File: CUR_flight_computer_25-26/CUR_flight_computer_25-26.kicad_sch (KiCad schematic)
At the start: 0 parts

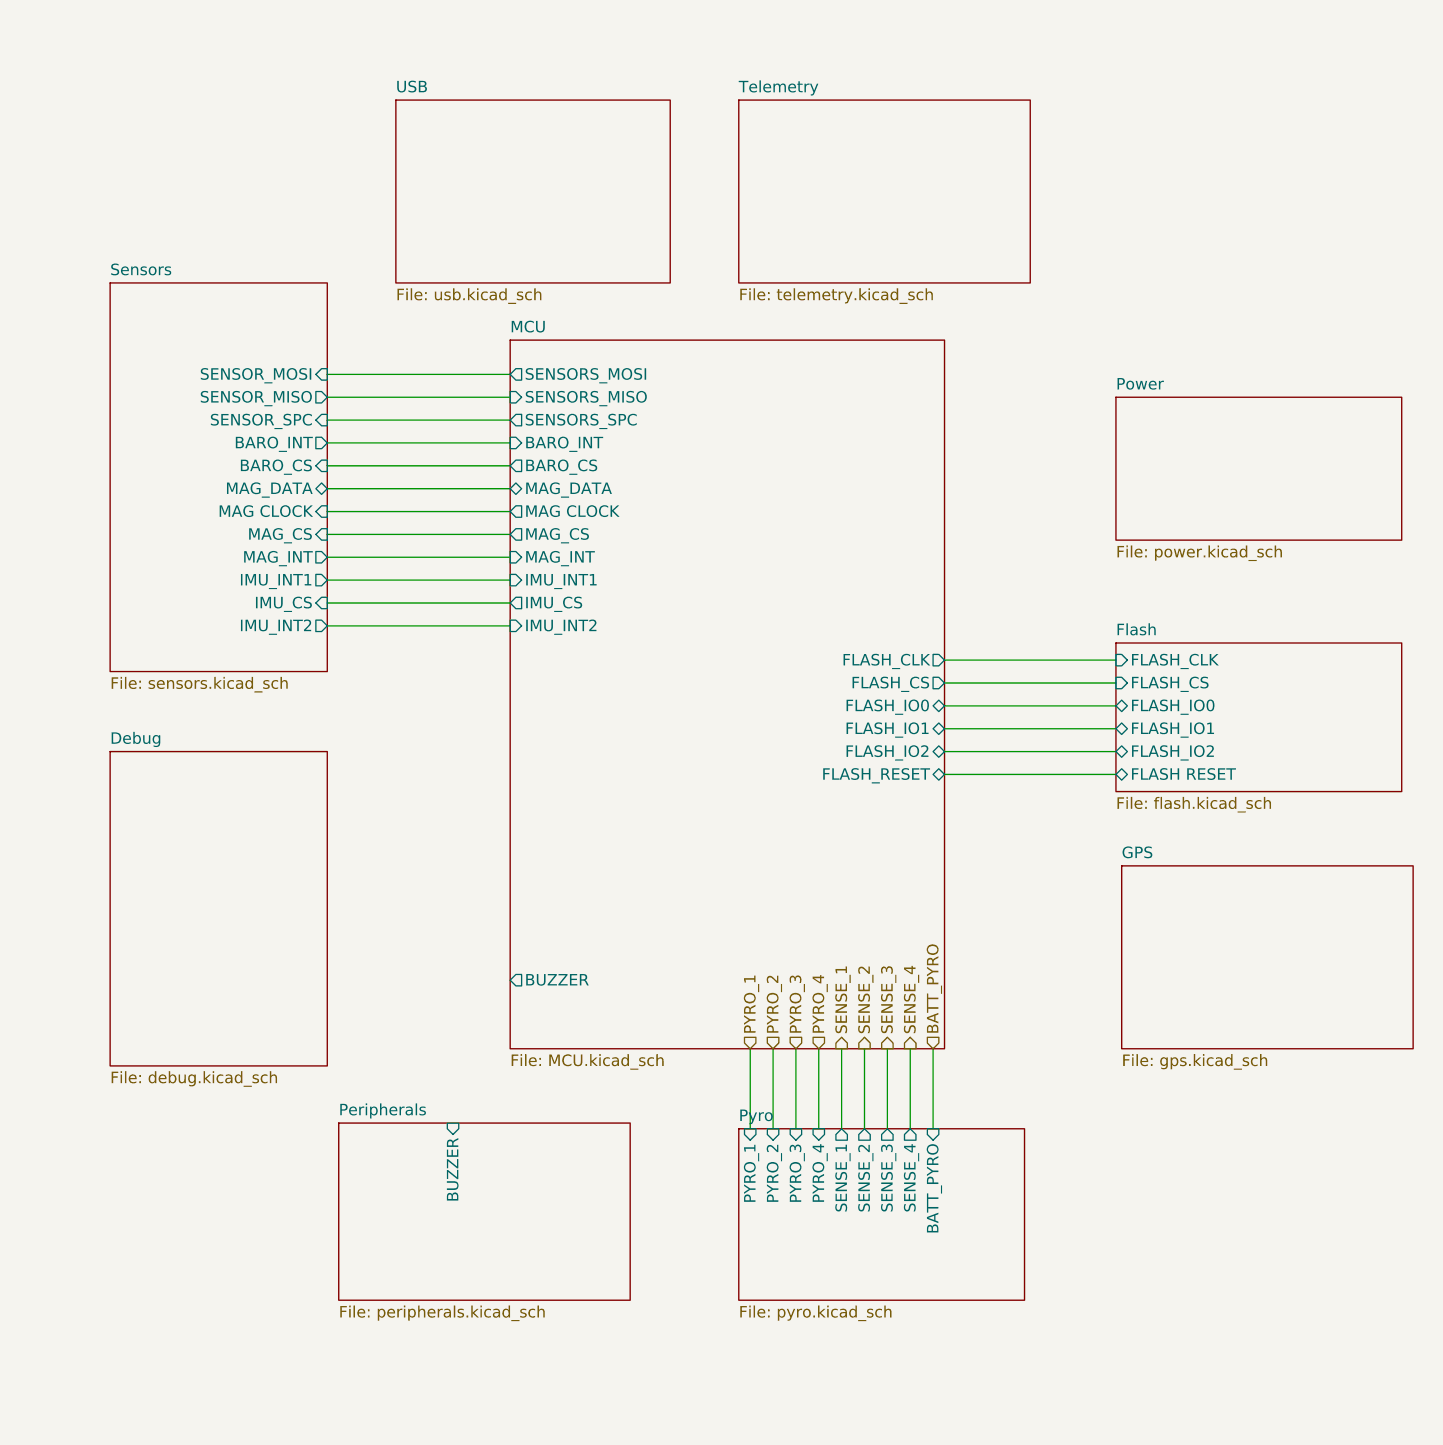
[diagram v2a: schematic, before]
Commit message: updated pins
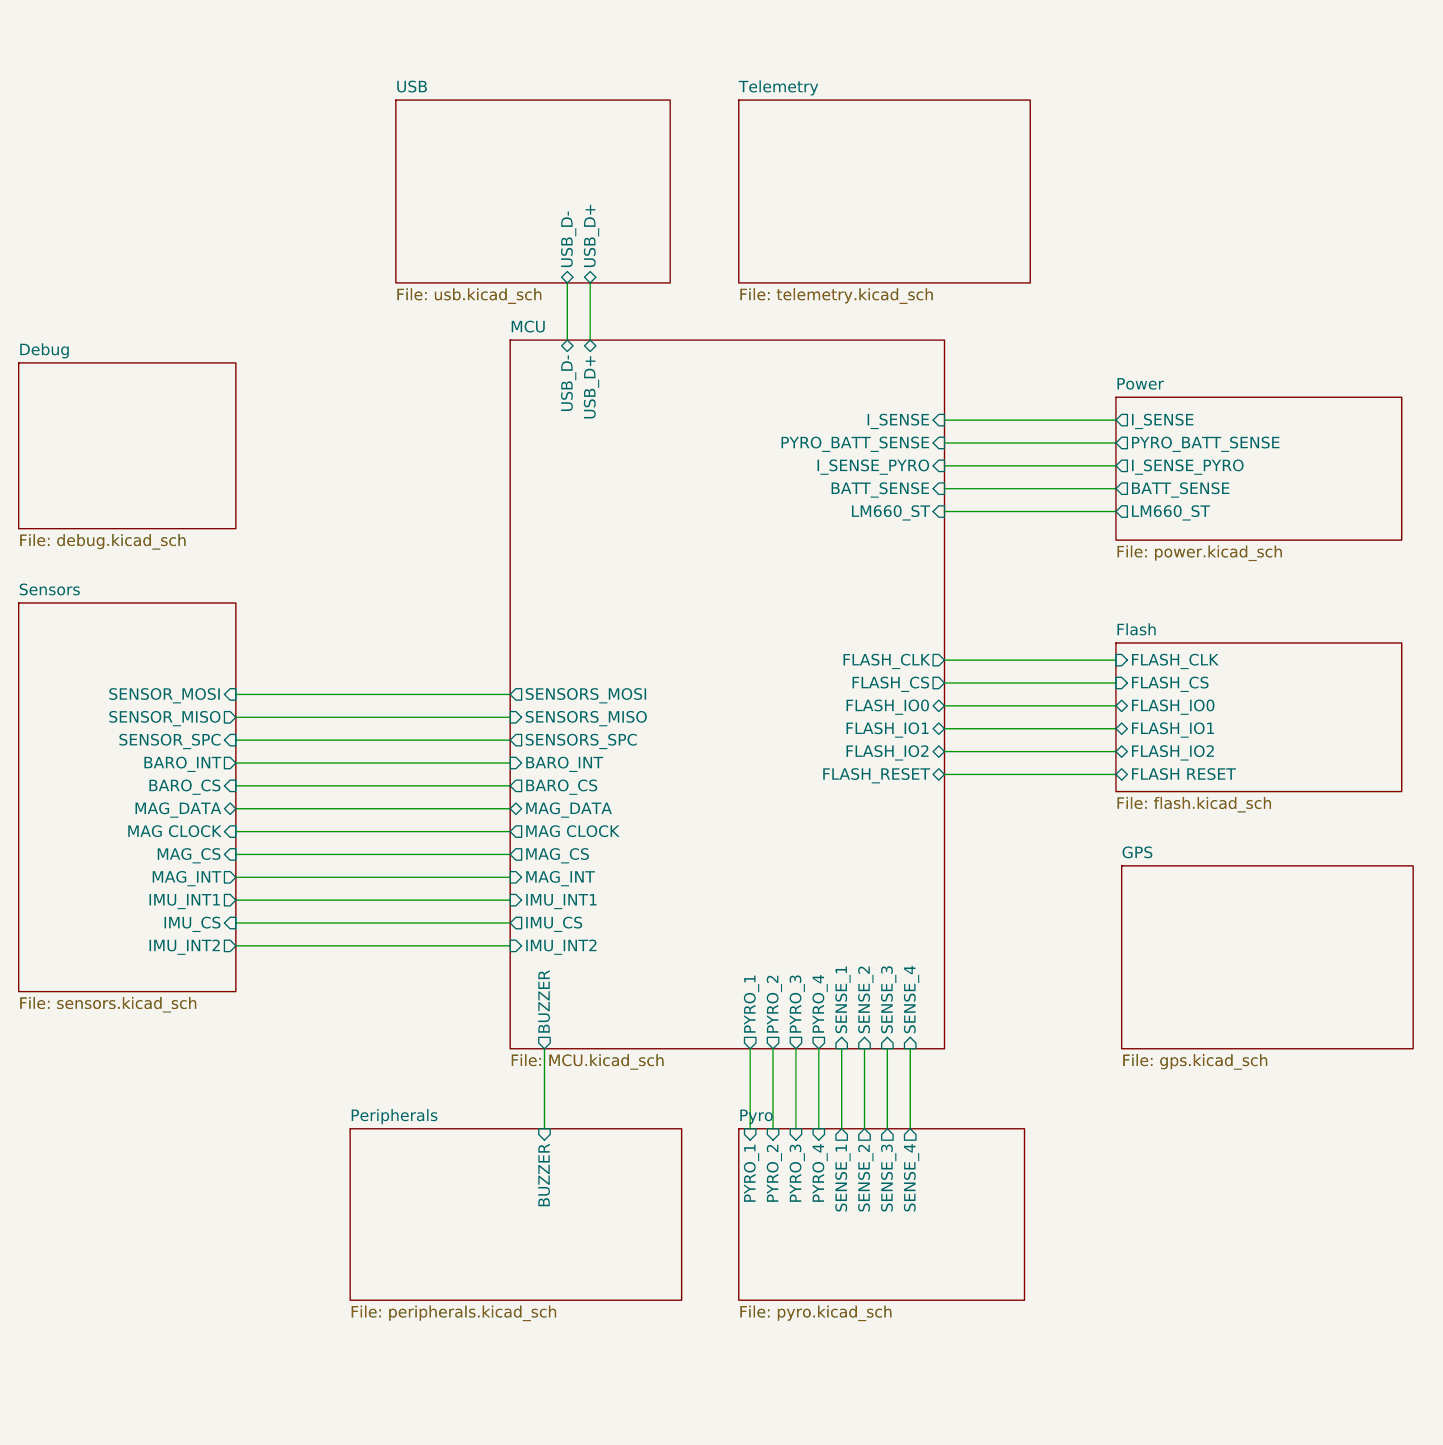
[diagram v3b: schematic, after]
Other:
- sheet MCU ports: added BATT_SENSE, I_SENSE, I_SENSE_PYRO, LM660_ST, PYRO_1, PYRO_2, PYRO_3, PYRO_4, PYRO_BATT_SENSE, SENSE_1, SENSE_2, SENSE_3, SENSE_4, USB_D+, USB_D-; removed none
- sheet Power ports: added BATT_SENSE, I_SENSE, I_SENSE_PYRO, LM660_ST, PYRO_BATT_SENSE; removed none
- sheet Pyro ports: added none; removed BATT_PYRO
- sheet USB ports: added USB_D+, USB_D-; removed none

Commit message: added rf pins
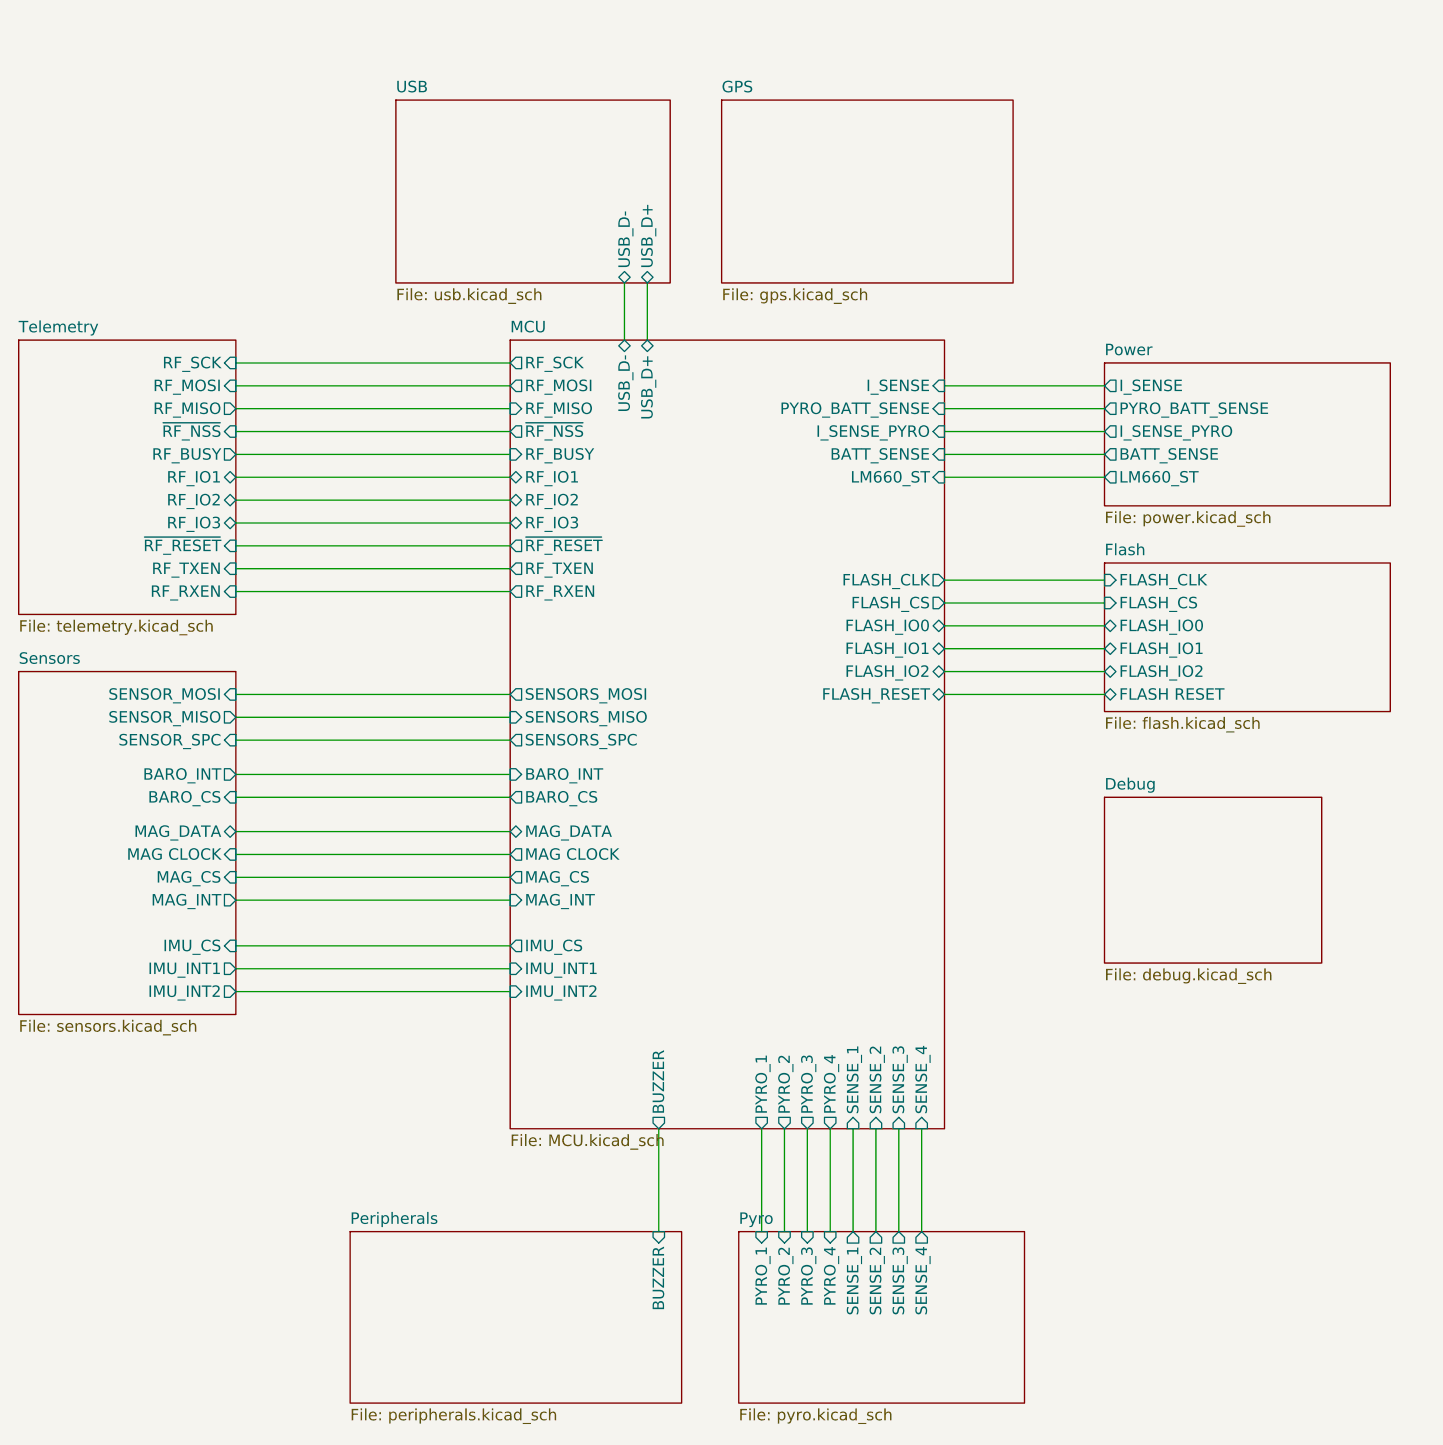
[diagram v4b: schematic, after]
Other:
- sheet MCU ports: added RF_BUSY, RF_IO1, RF_IO2, RF_IO3, RF_MISO, RF_MOSI, RF_RXEN, RF_SCK, RF_TXEN, ~{RF_NSS}, ~{RF_RESET}; removed none
- sheet Telemetry ports: added RF_BUSY, RF_IO1, RF_IO2, RF_IO3, RF_MISO, RF_MOSI, RF_RXEN, RF_SCK, RF_TXEN, ~{RF_NSS}, ~{RF_RESET}; removed none

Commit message: added gps pins
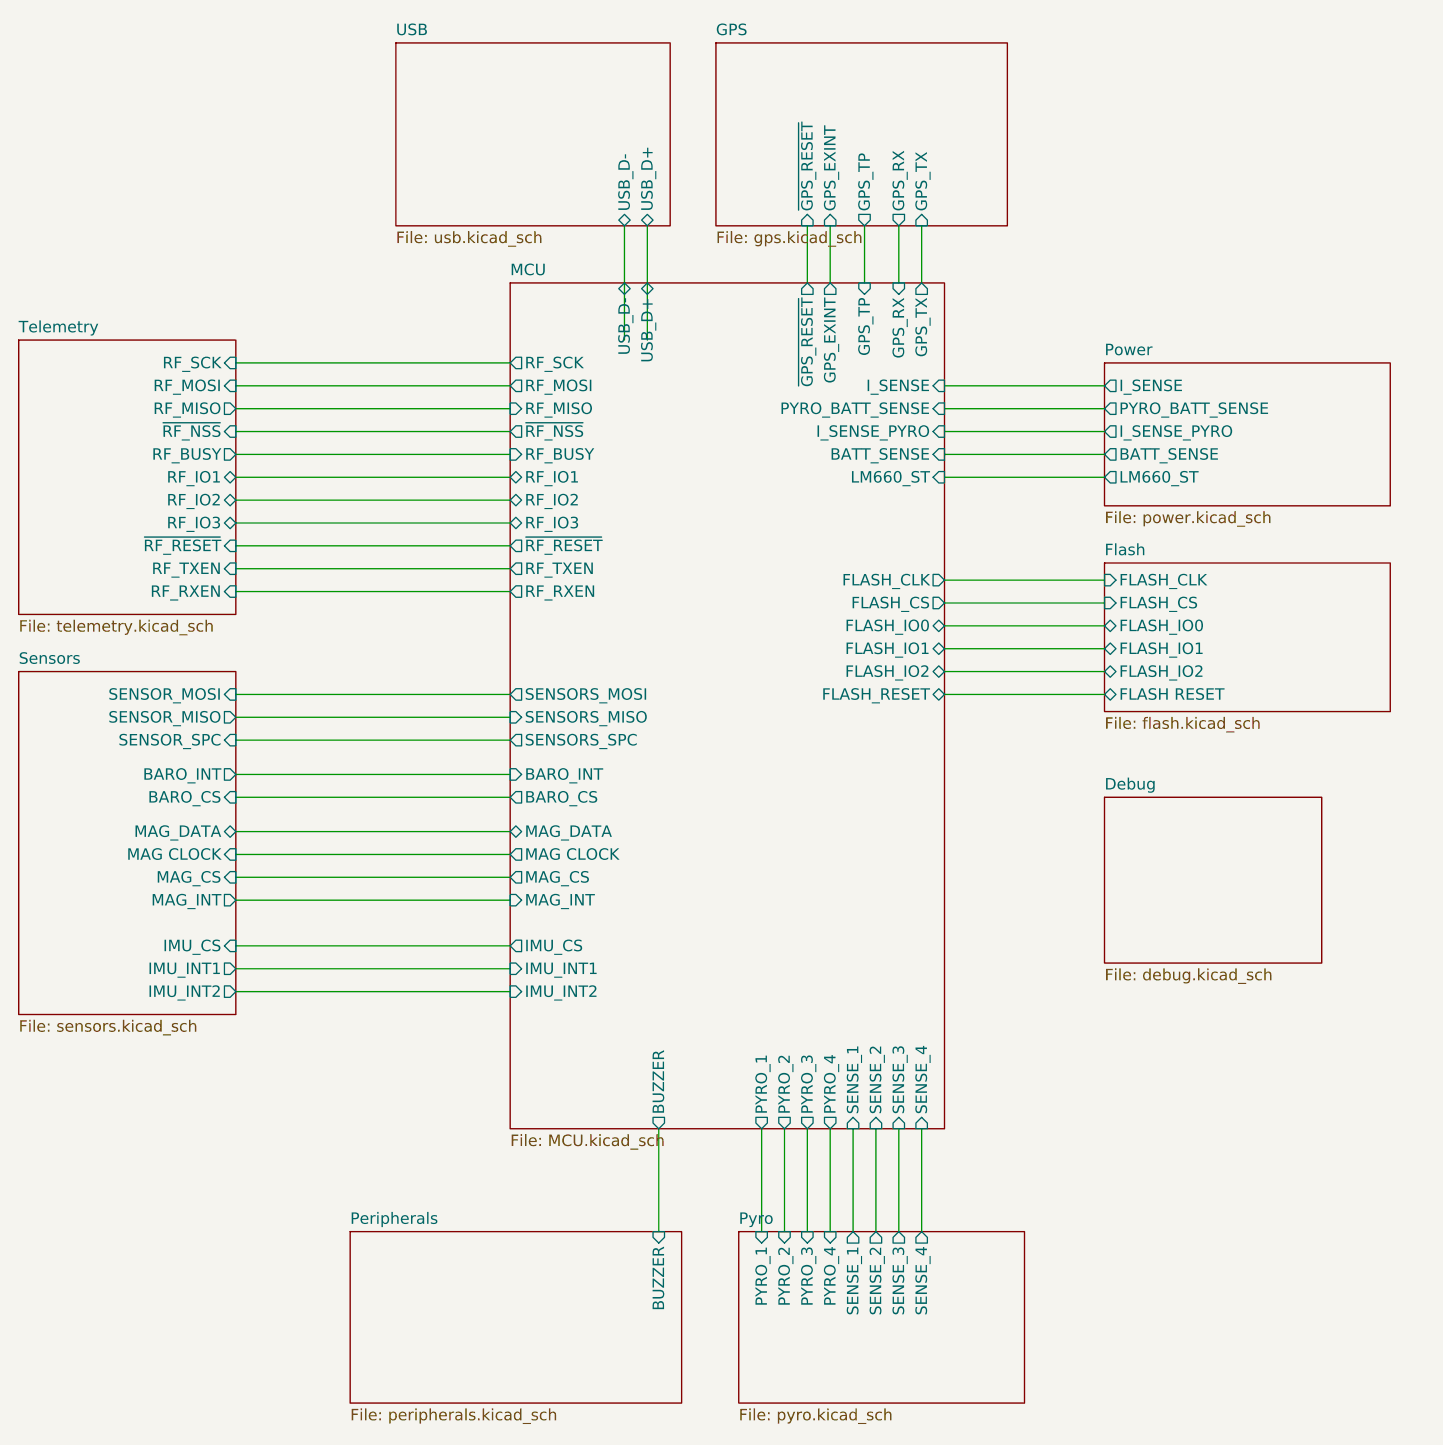
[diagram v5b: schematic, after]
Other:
- sheet GPS ports: added GPS_EXINT, GPS_RX, GPS_TP, GPS_TX, ~{GPS_RESET}; removed none
- sheet MCU ports: added GPS_EXINT, GPS_RX, GPS_TP, GPS_TX, ~{GPS_RESET}; removed none
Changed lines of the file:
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@@
+	(wire
+		(pts
+			(xy 157.48 39.37) (xy 157.48 45.72)
+		)
+		(stroke
+			(width 0)
+			(type default)
+		)
+	)
 	(wire
 		(pts
@@
 	(wire
 		(pts
-			(xy 129.54 45.72) (xy 129.54 52.07)
+			(xy 129.54 39.37) (xy 129.54 52.07)
 		)
 		(stroke
@@
 	(wire
 		(pts
+			(xy 147.32 39.37) (xy 147.32 45.72)
+		)
+		(stroke
+			(width 0)
+			(type default)
+		)
+	)
+	(wire
+		(pts
 			(xy 162.56 86.36) (xy 180.34 86.36)
 		)
@@
 	(wire
 		(pts
+			(xy 153.67 39.37) (xy 153.67 45.72)
+		)
+		(stroke
+			(width 0)
+			(type default)
+		)
+	)
+	(wire
+		(pts
 			(xy 83.82 57.15) (xy 114.3 57.15)
 		)
@@
 	(wire
 		(pts
+			(xy 149.86 39.37) (xy 149.86 45.72)
+		)
+		(stroke
+			(width 0)
+			(type default)
+		)
+	)
+	(wire
+		(pts
 			(xy 83.82 54.61) (xy 114.3 54.61)
 		)
@@
 	(wire
 		(pts
+			(xy 127 39.37) (xy 127 52.07)
+		)
+		(stroke
+			(width 0)
+			(type default)
+		)
+	)
+	(wire
+		(pts
 			(xy 162.56 83.82) (xy 180.34 83.82)
 		)
@@
 	(wire
 		(pts
-			(xy 127 45.72) (xy 127 52.07)
+			(xy 160.02 39.37) (xy 160.02 45.72)
 		)
 		(stroke
@@
 	)
 	(sheet
-		(at 114.3 52.07)
-		(size 48.26 87.63)
+		(at 114.3 45.72)
+		(size 48.26 93.98)
 		(exclude_from_sim no)
 		(in_bom yes)
@@
 		)
 		(property "Sheetname" "MCU"
-			(at 114.3 51.3584 0)
+			(at 114.3 45.0084 0)
 			(effects
 				(font
@@
 		)
 		(pin "USB_D-" bidirectional
-			(at 127 52.07 90)
+			(at 127 45.72 90)
 			(effects
 				(font
@@
 		)
 		(pin "USB_D+" bidirectional
-			(at 129.54 52.07 90)
+			(at 129.54 45.72 90)
 			(effects
 				(font
@@
 				)
 				(justify left)
+			)
+		)
+		(pin "GPS_RX" input
+			(at 157.48 45.72 90)
+			(effects
+				(font
+					(size 1.27 1.27)
+				)
+				(justify right)
+			)
+		)
+		(pin "~{GPS_RESET}" output
+			(at 147.32 45.72 90)
+			(effects
+				(font
+					(size 1.27 1.27)
+				)
+				(justify right)
+			)
+		)
+		(pin "GPS_TX" output
+			(at 160.02 45.72 90)
+			(effects
+				(font
+					(size 1.27 1.27)
+				)
+				(justify right)
+			)
+		)
+		(pin "GPS_TP" input
+			(at 153.67 45.72 90)
+			(effects
+				(font
+					(size 1.27 1.27)
+				)
+				(justify right)
+			)
+		)
+		(pin "GPS_EXINT" output
+			(at 149.86 45.72 90)
+			(effects
+				(font
+					(size 1.27 1.27)
+				)
+				(justify right)
 			)
 		)
@@
 	)
 	(sheet
-		(at 101.6 25.4)
+		(at 101.6 19.05)
 		(size 30.48 20.32)
 		(exclude_from_sim no)
@@
 		)
 		(property "Sheetname" "USB"
-			(at 101.6 24.6884 0)
+			(at 101.6 18.3384 0)
 			(effects
 				(font
@@
 		)
 		(property "Sheetfile" "usb.kicad_sch"
-			(at 101.6 46.3046 0)
+			(at 101.6 39.9546 0)
 			(effects
 				(font
@@
 		)
 		(pin "USB_D+" bidirectional
-			(at 129.54 45.72 270)
+			(at 129.54 39.37 270)
 			(effects
 				(font
@@
 		)
 		(pin "USB_D-" bidirectional
-			(at 127 45.72 270)
+			(at 127 39.37 270)
 			(effects
 				(font
@@
 	)
 	(sheet
-		(at 137.795 25.4)
+		(at 137.16 19.05)
 		(size 32.385 20.32)
 		(exclude_from_sim no)
@@
 		)
 		(property "Sheetname" "GPS"
-			(at 137.795 24.6884 0)
+			(at 137.16 18.3384 0)
 			(effects
 				(font
@@
 		)
 		(property "Sheetfile" "gps.kicad_sch"
-			(at 137.795 46.3046 0)
+			(at 137.16 39.9546 0)
 			(effects
 				(font
@@
 			)
 		)
+		(pin "GPS_TX" input
+			(at 160.02 39.37 270)
+			(effects
+				(font
+					(size 1.27 1.27)
+				)
+				(justify left)
+			)
+		)
+		(pin "GPS_TP" output
+			(at 153.67 39.37 270)
+			(effects
+				(font
+					(size 1.27 1.27)
+				)
+				(justify left)
+			)
+		)
+		(pin "GPS_EXINT" input
+			(at 149.86 39.37 270)
+			(effects
+				(font
+					(size 1.27 1.27)
+				)
+				(justify left)
+			)
+		)
+		(pin "~{GPS_RESET}" input
+			(at 147.32 39.37 270)
+			(effects
+				(font
+					(size 1.27 1.27)
+				)
+				(justify left)
+			)
+		)
+		(pin "GPS_RX" output
+			(at 157.48 39.37 270)
+			(effects
+				(font
+					(size 1.27 1.27)
+				)
+				(justify left)
+			)
+		)
